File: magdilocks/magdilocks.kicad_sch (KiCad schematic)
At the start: 11 parts, among them J1 Conn_1x4, J2 Conn_1x4, J3 Conn_1x3, U1 U_DRV5053, U2 U_Si7210

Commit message: Initial design
Commit of v1.0 design and fabrication files
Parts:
- removed J1, J2: Conn_1x4, symbol master-vampire:Conn_1x4
- added J2, J3: Conn_1x3, master-vampire:CONN_HEADER_MALE_1X3PIN_P1.27MM_TH, symbol master-vampire:Conn_1x3
- C1: footprint (none) -> master-vampire:C_0805; Capacitance 1uF -> 0.047uF; MPN DNP -> CL21B473KBCNNNC; Manufacturer DNP -> Samsung Electro-Mechanics; Package 0603 -> 0805; Supplier DNP -> DigiKey; Variant_DRV (none) -> DNP
- C2: footprint (none) -> master-vampire:C_0805; Capacitance 1uF -> 100nF; LCSC (none) -> C695378; MPN DNP -> CL21B104KACNNNC; Manufacturer DNP -> Samsung Electro-Mechanics; Package 0603 -> 0805; Supplier DNP -> DigiKey; Supplier PN DNP -> 1276-1099-1-ND; Variant_Si7210 (none) -> DNP
- J1: renamed from J3; footprint (none) -> master-vampire:CONN_HEADER_MALE_1X3PIN_P1.27MM_TH_Phob; MPN DNP -> GRPB031VWVN-RC; Manufacturer DNP -> Sullins Connector Solutions; Package DNP -> Through-hole; Supplier (none) -> DigiKey; Supplier PN (none) -> S9014E-03-ND; Variant_Si7210 (none) -> DNP
- R1, R2, R3: footprint (none) -> master-vampire:R_0805; LCSC (none) -> C269724; MPN DNP -> RNCP0805FTD10K0; MV PN (none) -> DNP; Manufacturer DNP -> Stackpole Electronics Inc; Package 0603 -> 0805; Supplier DNP -> DigiKey; Tolerance 5% -> 5per; Variant_DRV (none) -> DNP
- R4: footprint (none) -> master-vampire:R_0805; LCSC (none) -> C186482; MPN DNP -> CRG0805F2K0; MV PN (none) -> DNP; Manufacturer DNP -> TE Connectivity Passive Product; Package 0603 -> 0805; Resistance 10k -> 2k; Supplier DNP -> DigiKey; Tolerance 5% -> 5per; Variant_DRV (none) -> DNP
- U1: footprint (none) -> master-vampire:SOT-23-3; MPN DRV5053xx -> DRV5053PAQDBZTQ1; Package DNP -> SOT-23-3; Supplier DNP -> DigiKey; Supplier PN DNP -> 296-DRV5053PAQDBZTQ1CT-ND; Variant_Si7210 (none) -> DNP
- U2: footprint (none) -> master-vampire:SOT-23-5; MPN Si7210xx -> SI7210-B-00-IV; Package DNP -> SOT-23-5; Supplier DNP -> DigiKey; Variant_DRV (none) -> DNP
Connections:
- net ALERT is gone; now on net OUT_RAW: R1.2, U2.5 (ALERT)
- net +3V3: now also J2.1
- net GND: now also J3.3
- net OUT_FLT: now also J2.2
- net OUT_RAW: now also J2.3
- net SCL: now also J3.2
- net SDA: now also J3.1
- no-connect marks 1 -> 0

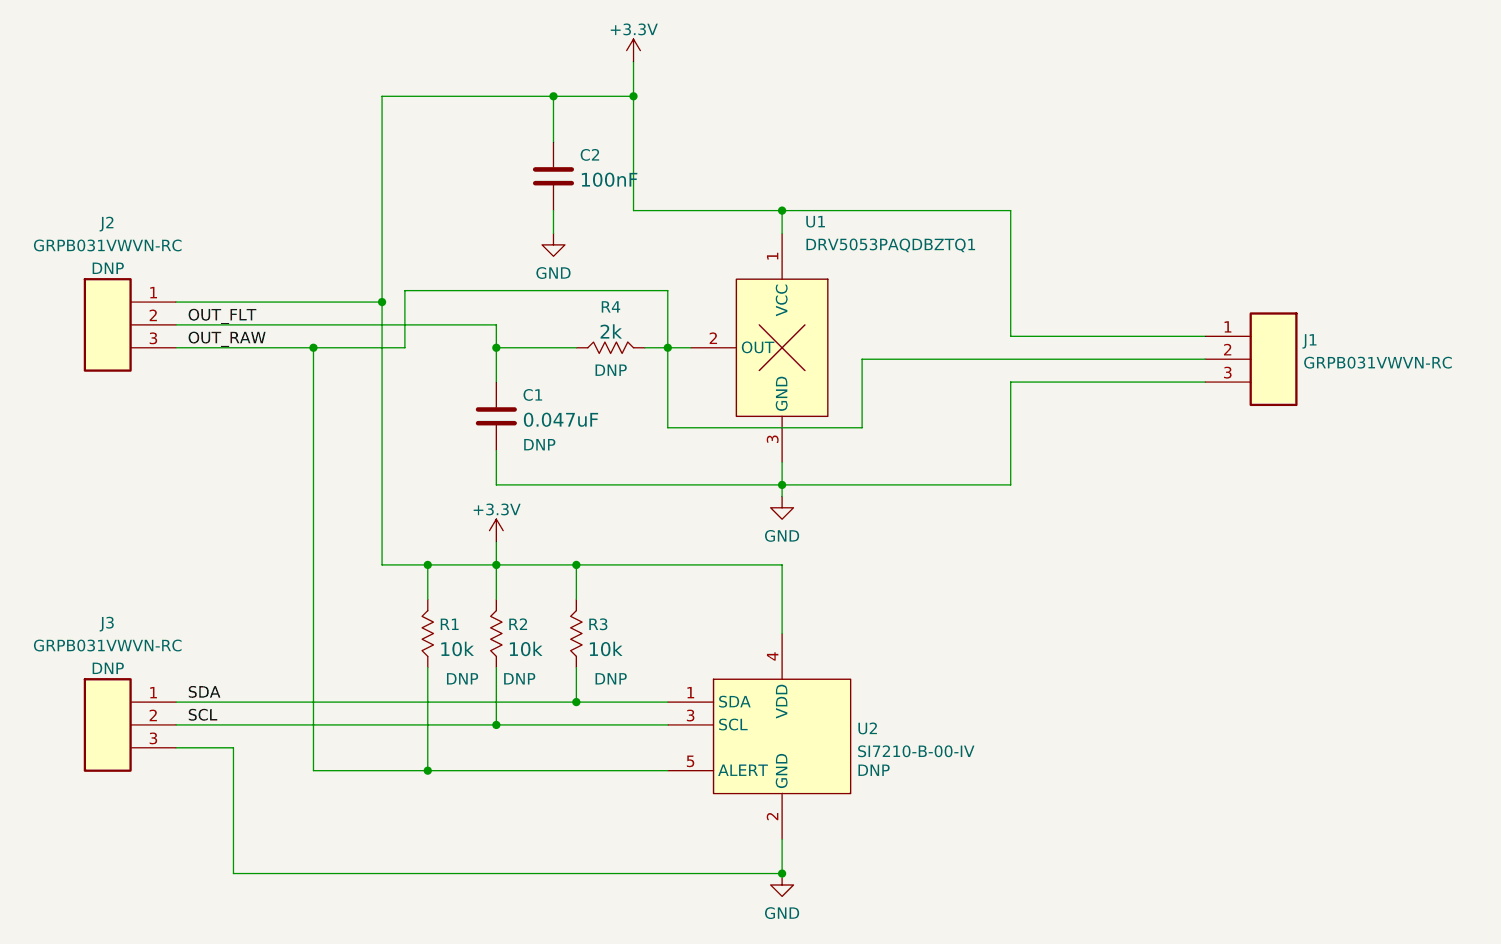
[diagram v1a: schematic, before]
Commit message: v2.0 Release
Modified board shape to fit on Phob 1.2.2. Changed pin assignments for development headers.
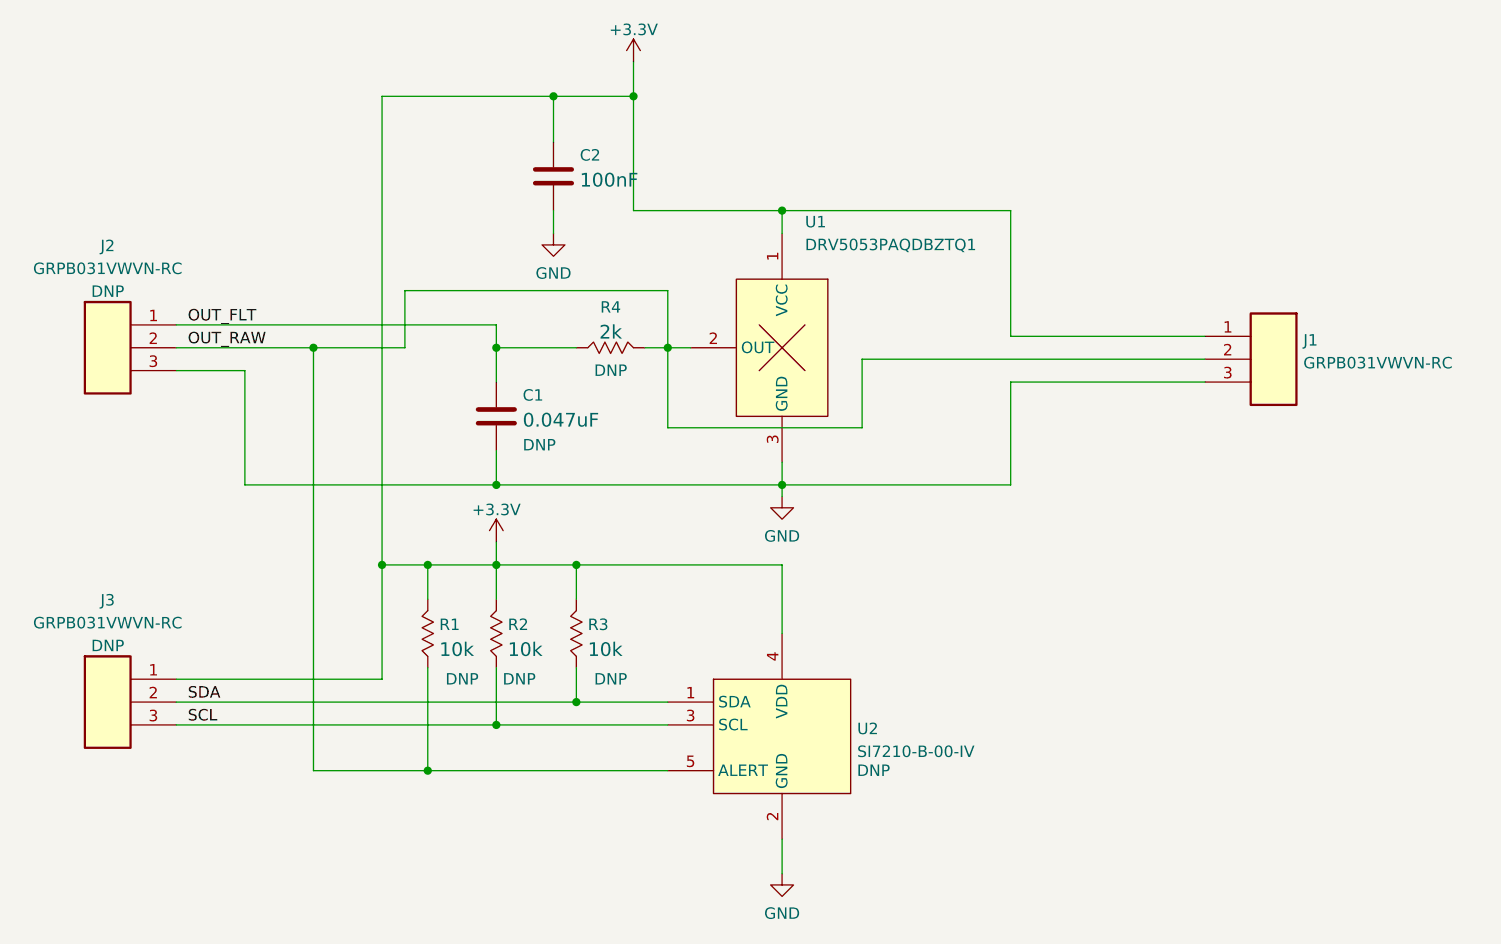
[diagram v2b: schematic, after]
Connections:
- net +3V3: now also J3.1; no longer J2.1
- net GND: now also J2.3; no longer J3.3
- net OUT_FLT: now also J2.1; no longer J2.2
- net OUT_RAW: now also J2.2; no longer J2.3
- net SCL: now also J3.3; no longer J3.2
- net SDA: now also J3.2; no longer J3.1
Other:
- moved on the sheet: J2, J3
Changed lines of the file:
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@@
   (junction (at 113.03 128.27) (diameter 0) (color 0 0 0 0)
   )
-  (junction (at 152.4 139.7) (diameter 0) (color 0 0 0 0)
-  )
   (junction (at 139.7 81.28) (diameter 0) (color 0 0 0 0)
   )
@@
   (junction (at 127 53.34) (diameter 0) (color 0 0 0 0)
   )
-  (junction (at 107.95 76.2) (diameter 0) (color 0 0 0 0)
+  (junction (at 120.65 96.52) (diameter 0) (color 0 0 0 0)
+  )
+  (junction (at 107.95 105.41) (diameter 0) (color 0 0 0 0)
   )
   (junction (at 152.4 66.04) (diameter 0) (color 0 0 0 0)
@@
     (stroke (width 0) (type default) (color 0 0 0 0))
   )
+  (wire (pts (xy 92.71 83.82) (xy 92.71 96.52))
+    (stroke (width 0) (type default) (color 0 0 0 0))
+  )
   (wire (pts (xy 100.33 81.28) (xy 100.33 128.27))
     (stroke (width 0) (type default) (color 0 0 0 0))
@@
     (stroke (width 0) (type default) (color 0 0 0 0))
   )
-  (wire (pts (xy 91.44 139.7) (xy 152.4 139.7))
-    (stroke (width 0) (type default) (color 0 0 0 0))
-  )
   (wire (pts (xy 85.09 81.28) (xy 100.33 81.28))
     (stroke (width 0) (type default) (color 0 0 0 0))
@@
     (stroke (width 0) (type default) (color 0 0 0 0))
   )
+  (wire (pts (xy 85.09 118.11) (xy 107.95 118.11))
+    (stroke (width 0) (type default) (color 0 0 0 0))
+  )
   (wire (pts (xy 129.54 105.41) (xy 120.65 105.41))
     (stroke (width 0) (type default) (color 0 0 0 0))
   )
+  (wire (pts (xy 85.09 83.82) (xy 92.71 83.82))
+    (stroke (width 0) (type default) (color 0 0 0 0))
+  )
   (wire (pts (xy 199.39 82.55) (xy 161.29 82.55))
     (stroke (width 0) (type default) (color 0 0 0 0))
@@
     (stroke (width 0) (type default) (color 0 0 0 0))
   )
+  (wire (pts (xy 107.95 118.11) (xy 107.95 105.41))
+    (stroke (width 0) (type default) (color 0 0 0 0))
+  )
   (wire (pts (xy 120.65 123.19) (xy 120.65 116.84))
     (stroke (width 0) (type default) (color 0 0 0 0))
   )
-  (wire (pts (xy 85.09 125.73) (xy 91.44 125.73))
-    (stroke (width 0) (type default) (color 0 0 0 0))
-  )
-  (wire (pts (xy 107.95 76.2) (xy 107.95 53.34))
+  (wire (pts (xy 107.95 53.34) (xy 107.95 105.41))
     (stroke (width 0) (type default) (color 0 0 0 0))
   )
@@
     (stroke (width 0) (type default) (color 0 0 0 0))
   )
-  (wire (pts (xy 85.09 76.2) (xy 107.95 76.2))
-    (stroke (width 0) (type default) (color 0 0 0 0))
-  )
   (wire (pts (xy 139.7 81.28) (xy 142.24 81.28))
     (stroke (width 0) (type default) (color 0 0 0 0))
   )
-  (wire (pts (xy 107.95 105.41) (xy 107.95 76.2))
-    (stroke (width 0) (type default) (color 0 0 0 0))
-  )
   (wire (pts (xy 120.65 105.41) (xy 120.65 109.22))
     (stroke (width 0) (type default) (color 0 0 0 0))
@@
     (stroke (width 0) (type default) (color 0 0 0 0))
   )
+  (wire (pts (xy 92.71 96.52) (xy 120.65 96.52))
+    (stroke (width 0) (type default) (color 0 0 0 0))
+  )
   (wire (pts (xy 177.8 80.01) (xy 177.8 66.04))
     (stroke (width 0) (type default) (color 0 0 0 0))
@@
   )
   (wire (pts (xy 135.89 49.53) (xy 135.89 53.34))
-    (stroke (width 0) (type default) (color 0 0 0 0))
-  )
-  (wire (pts (xy 91.44 125.73) (xy 91.44 139.7))
     (stroke (width 0) (type default) (color 0 0 0 0))
   )
@@
     (pin "3")
   )
-  (symbol (lib_id "master-vampire:Conn_1x3") (at 77.47 123.19 0) (unit 1)
-    (in_bom yes) (on_board yes) (fields_autoplaced)
-    (property "Reference" "J3" (id 0) (at 77.47 111.8734 0))
-    (property "Value" "Conn_1x3" (id 1) (at 91.44 115.57 0)
-      (effects (font (size 1.27 1.27)) hide)
-    )
-    (property "Footprint" "master-vampire:CONN_HEADER_MALE_1X3PIN_P1.27MM_TH" (id 2) (at 77.47 123.19 0)
-      (effects (font (size 1.27 1.27)) hide)
-    )
-    (property "Datasheet" "" (id 3) (at 77.47 123.19 0)
-      (effects (font (size 1.27 1.27)) hide)
-    )
-    (property "Manufacturer" "Sullins Connector Solutions" (id 4) (at 77.47 123.19 0)
-      (effects (font (size 1.27 1.27)) hide)
-    )
-    (property "MPN" "GRPB031VWVN-RC" (id 5) (at 77.47 114.4103 0))
-    (property "MV PN" "DNP" (id 6) (at 77.47 116.9472 0))
-    (property "Package" "Through-Hole" (id 7) (at 77.47 123.19 0)
-      (effects (font (size 1.27 1.27)) hide)
-    )
-    (property "Supplier" "DigiKey" (id 8) (at 77.47 123.19 0)
-      (effects (font (size 1.27 1.27)) hide)
-    )
-    (property "Supplier PN" "DNP" (id 9) (at 77.47 123.19 0)
-      (effects (font (size 1.27 1.27)) hide)
-    )
-    (property "Variant_DRV" "DNP" (id 10) (at 77.47 123.19 0)
-      (effects (font (size 1.27 1.27)) hide)
-    )
-    (property "Variant_Si7210" "~" (id 11) (at 77.47 123.19 0)
+  (symbol (lib_id "master-vampire:Conn_1x3") (at 77.47 120.65 0) (unit 1)
+    (in_bom yes) (on_board yes) (fields_autoplaced)
+    (property "Reference" "J3" (id 0) (at 77.47 109.3334 0))
+    (property "Value" "Conn_1x3" (id 1) (at 91.44 113.03 0)
+      (effects (font (size 1.27 1.27)) hide)
+    )
+    (property "Footprint" "master-vampire:CONN_HEADER_MALE_1X3PIN_P1.27MM_TH" (id 2) (at 77.47 120.65 0)
+      (effects (font (size 1.27 1.27)) hide)
+    )
+    (property "Datasheet" "" (id 3) (at 77.47 120.65 0)
+      (effects (font (size 1.27 1.27)) hide)
+    )
+    (property "Manufacturer" "Sullins Connector Solutions" (id 4) (at 77.47 120.65 0)
+      (effects (font (size 1.27 1.27)) hide)
+    )
+    (property "MPN" "GRPB031VWVN-RC" (id 5) (at 77.47 111.8703 0))
+    (property "MV PN" "DNP" (id 6) (at 77.47 114.4072 0))
+    (property "Package" "Through-Hole" (id 7) (at 77.47 120.65 0)
+      (effects (font (size 1.27 1.27)) hide)
+    )
+    (property "Supplier" "DigiKey" (id 8) (at 77.47 120.65 0)
+      (effects (font (size 1.27 1.27)) hide)
+    )
+    (property "Supplier PN" "DNP" (id 9) (at 77.47 120.65 0)
+      (effects (font (size 1.27 1.27)) hide)
+    )
+    (property "Variant_DRV" "DNP" (id 10) (at 77.47 120.65 0)
+      (effects (font (size 1.27 1.27)) hide)
+    )
+    (property "Variant_Si7210" "~" (id 11) (at 77.47 120.65 0)
       (effects (font (size 1.27 1.27)) hide)
     )
@@
     (pin "1")
   )
-  (symbol (lib_id "master-vampire:Conn_1x3") (at 77.47 78.74 0) (unit 1)
-    (in_bom yes) (on_board yes) (fields_autoplaced)
-    (property "Reference" "J2" (id 0) (at 77.47 67.4234 0))
-    (property "Value" "Conn_1x3" (id 1) (at 91.44 71.12 0)
-      (effects (font (size 1.27 1.27)) hide)
-    )
-    (property "Footprint" "master-vampire:CONN_HEADER_MALE_1X3PIN_P1.27MM_TH" (id 2) (at 77.47 78.74 0)
-      (effects (font (size 1.27 1.27)) hide)
-    )
-    (property "Datasheet" "" (id 3) (at 77.47 78.74 0)
-      (effects (font (size 1.27 1.27)) hide)
-    )
-    (property "Manufacturer" "Sullins Connector Solutions" (id 4) (at 77.47 78.74 0)
-      (effects (font (size 1.27 1.27)) hide)
-    )
-    (property "MPN" "GRPB031VWVN-RC" (id 5) (at 77.47 69.9603 0))
-    (property "MV PN" "DNP" (id 6) (at 77.47 72.4972 0))
-    (property "Package" "Through-Hole" (id 7) (at 77.47 78.74 0)
-      (effects (font (size 1.27 1.27)) hide)
-    )
-    (property "Supplier" "DigiKey" (id 8) (at 77.47 78.74 0)
-      (effects (font (size 1.27 1.27)) hide)
-    )
-    (property "Supplier PN" "DNP" (id 9) (at 77.47 78.74 0)
-      (effects (font (size 1.27 1.27)) hide)
-    )
-    (property "Variant_DRV" "DNP" (id 10) (at 77.47 78.74 0)
-      (effects (font (size 1.27 1.27)) hide)
-    )
-    (property "Variant_Si7210" "~" (id 11) (at 77.47 78.74 0)
-      (effects (font (size 1.27 1.27)) hide)
-    )
+  (symbol (lib_id "master-vampire:Conn_1x3") (at 77.47 81.28 0) (unit 1)
+    (in_bom yes) (on_board yes) (fields_autoplaced)
+    (property "Reference" "J2" (id 0) (at 77.47 69.9634 0))
+    (property "Value" "Conn_1x3" (id 1) (at 91.44 73.66 0)
+      (effects (font (size 1.27 1.27)) hide)
+    )
+    (property "Footprint" "master-vampire:CONN_HEADER_MALE_1X3PIN_P1.27MM_TH" (id 2) (at 77.47 81.28 0)
+      (effects (font (size 1.27 1.27)) hide)
+    )
+    (property "Datasheet" "" (id 3) (at 77.47 81.28 0)
+      (effects (font (size 1.27 1.27)) hide)
+    )
+    (property "Manufacturer" "Sullins Connector Solutions" (id 4) (at 77.47 81.28 0)
+      (effects (font (size 1.27 1.27)) hide)
+    )
+    (property "MPN" "GRPB031VWVN-RC" (id 5) (at 77.47 72.5003 0))
+    (property "MV PN" "DNP" (id 6) (at 77.47 75.0372 0))
+    (property "Package" "Through-Hole" (id 7) (at 77.47 81.28 0)
+      (effects (font (size 1.27 1.27)) hide)
+    )
+    (property "Supplier" "DigiKey" (id 8) (at 77.47 81.28 0)
+      (effects (font (size 1.27 1.27)) hide)
+    )
+    (property "Supplier PN" "DNP" (id 9) (at 77.47 81.28 0)
+      (effects (font (size 1.27 1.27)) hide)
+    )
+    (property "Variant_DRV" "DNP" (id 10) (at 77.47 81.28 0)
+      (effects (font (size 1.27 1.27)) hide)
+    )
+    (property "Variant_Si7210" "~" (id 11) (at 77.47 81.28 0)
+      (effects (font (size 1.27 1.27)) hide)
+    )

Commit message: V2.0 production release
Fixed board shape to fit main board and c-stick PBCs. Created gerber/drill files, BOM export, 3D model, and render examples on Phob 1.2.2.
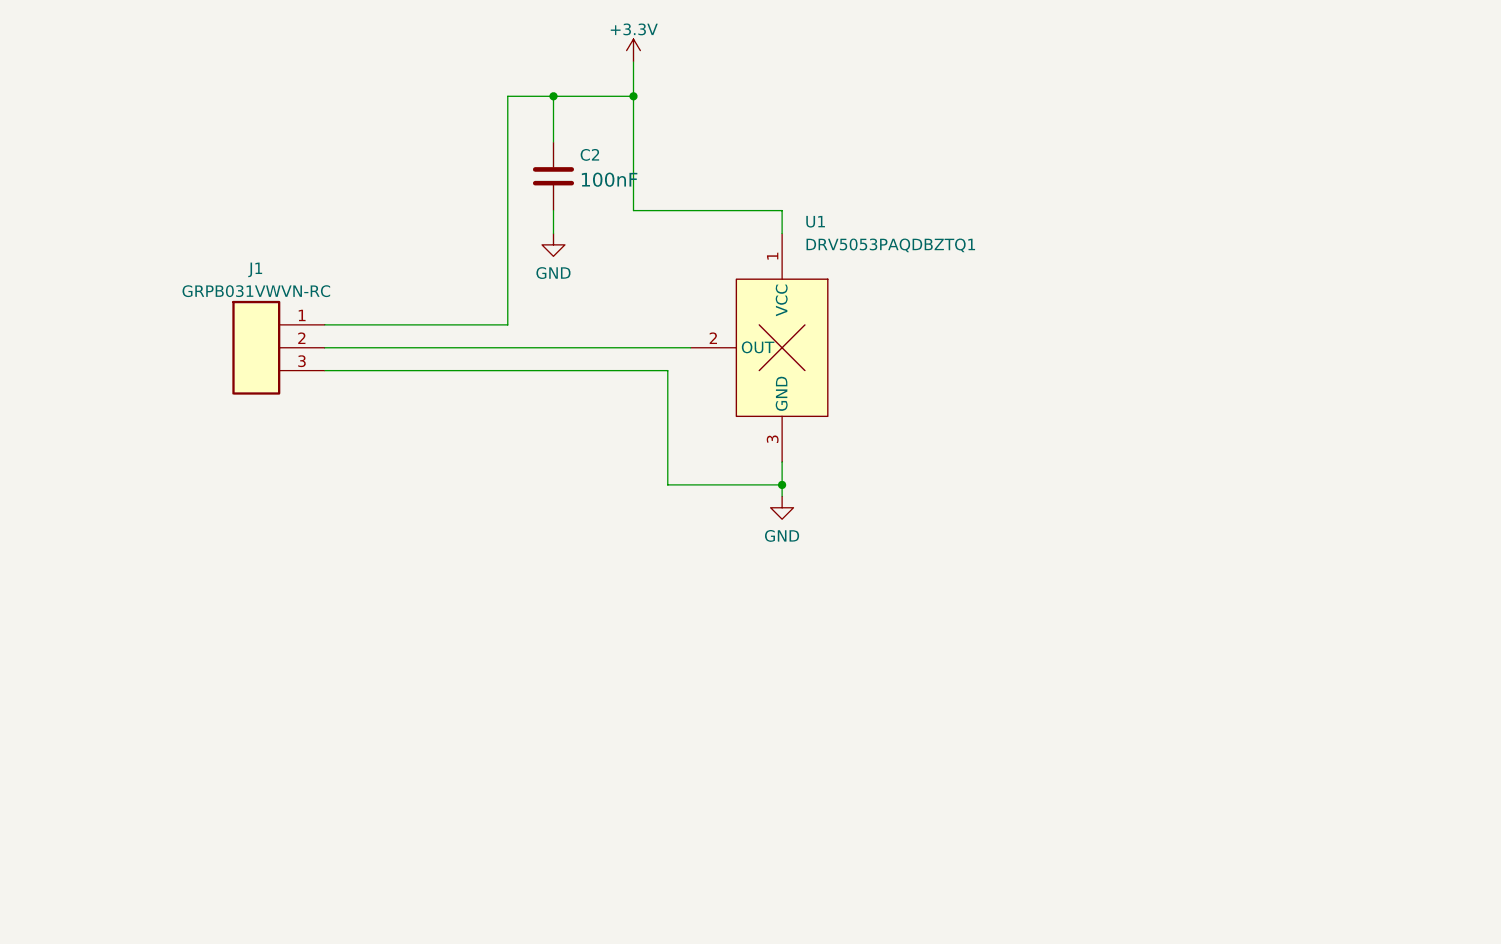
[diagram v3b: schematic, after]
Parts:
- removed C1: C, master-vampire:C_0805, symbol master-vampire:C
- removed J2, J3: Conn_1x3, master-vampire:CONN_HEADER_MALE_1X3PIN_P1.27MM_TH, symbol master-vampire:Conn_1x3
- removed R1, R2, R3, R4: R, master-vampire:R_0805, symbol master-vampire:R
- removed U2: U_Si7210, master-vampire:SOT-23-5, symbol master-vampire:U_Si7210
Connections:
- net OUT_RAW: no longer names the net of J1.2, U1.2 (OUT)
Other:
- moved on the sheet: J1
